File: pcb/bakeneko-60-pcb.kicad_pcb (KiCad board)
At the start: 2 copper layers, 284.8 x 106.7 mm, 150 parts, among them J1 JST SH 4-pin, J2 AVR-ISP-6, SW1 Reset, U1 SRV05-4, U2 ATmega32U4-AU, Y1 16MHz

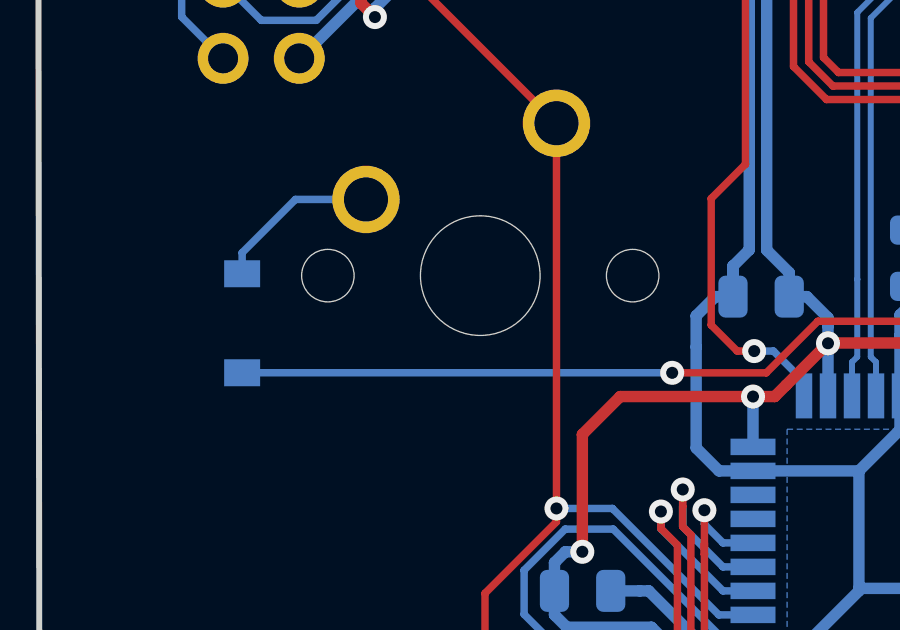
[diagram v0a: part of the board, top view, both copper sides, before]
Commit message: move diode and make room for jst replacement
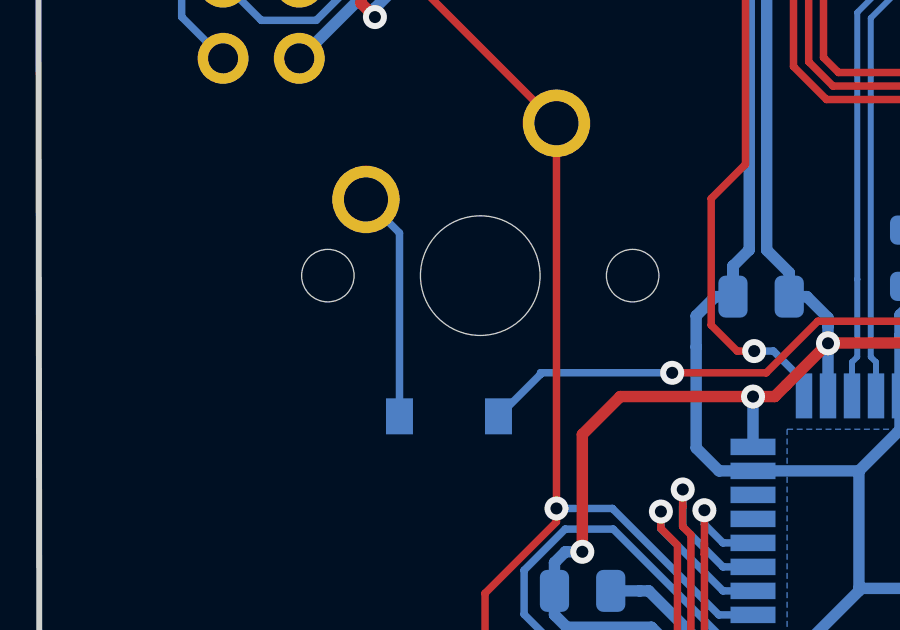
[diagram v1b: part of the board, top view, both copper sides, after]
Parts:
- moved D16 7.56 mm to (12.7, 32.7), turned to 180 degrees
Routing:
- net ROW1: track 261.0 -> 253.1 mm
- net Net-(D16-Pad2): track 5.56 -> 7.69 mm
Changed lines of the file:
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@@
   )
   (footprint "Diode_SMD:D_SOD-123" (layer "B.Cu")
-    (at 5.825 29.6375 90)
+    (at 12.72 32.74 180)
     (descr "SOD-123")
     (tags "SOD-123")
@@
     (property "Sheetname" "Switch Matrix")
     (attr smd)
-    (fp_text reference "D16" (at 0 -2 90) (layer "Dwgs.User")
+    (fp_text reference "D16" (at 0 -2) (layer "Dwgs.User")
       (effects (font (size 1 1) (thickness 0.15)) (justify mirror))
     )
-    (fp_text value "1N4148" (at 0 -2.1 90) (layer "B.Fab")
+    (fp_text value "1N4148" (at 0 -2.1) (layer "B.Fab")
       (effects (font (size 1 1) (thickness 0.15)) (justify mirror))
     )
-    (fp_text user "${REFERENCE}" (at 0 2 90) (layer "B.Fab")
+    (fp_text user "${REFERENCE}" (at 0 2) (layer "B.Fab")
       (effects (font (size 1 1) (thickness 0.15)) (justify mirror))
     )
@@
     (fp_line (start 1.4 0.9) (end 1.4 -0.9) (layer "B.Fab") (width 0.1))
     (fp_line (start -0.35 0) (end -0.35 -0.55) (layer "B.Fab") (width 0.1))
-    (pad "1" smd rect locked (at -1.65 0 90) (size 0.9 1.2) (layers "B.Cu" "B.Paste" "B.Mask")
+    (pad "1" smd rect locked (at -1.65 0 180) (size 0.9 1.2) (layers "B.Cu" "B.Paste" "B.Mask")
       (net 22 "ROW1") (pinfunction "K") (pintype "passive"))
-    (pad "2" smd rect locked (at 1.65 0 90) (size 0.9 1.2) (layers "B.Cu" "B.Paste" "B.Mask")
+    (pad "2" smd rect locked (at 1.65 0 180) (size 0.9 1.2) (layers "B.Cu" "B.Paste" "B.Mask")
       (net 20 "Net-(D16-Pad2)") (pinfunction "A") (pintype "passive"))
     (model "${KISYS3DMOD}/Diode_SMD.3dshapes/D_SOD-123.wrl"
@@
   (segment (start 258.55375 6.46) (end 256.49375 4.4) (width 0.25) (layer "B.Cu") (net 19))
   (segment (start 256.49375 4.4) (end 248.29375 4.4) (width 0.25) (layer "B.Cu") (net 19))
-  (segment (start 9.9525 25.51) (end 7.6025 25.51) (width 0.25) (layer "B.Cu") (net 20))
-  (segment (start 7.6025 25.51) (end 5.825 27.2875) (width 0.25) (layer "B.Cu") (net 20))
-  (segment (start 5.825 27.2875) (end 5.825 27.9875) (width 0.25) (layer "B.Cu") (net 20))
+  (segment (start 11.07 32.74) (end 11.07 26.6275) (width 0.25) (layer "B.Cu") (net 20))
+  (segment (start 11.07 26.6275) (end 9.9525 25.51) (width 0.25) (layer "B.Cu") (net 20))
   (segment (start 50.47375 25.51) (end 35.35599 25.51) (width 0.25) (layer "B.Cu") (net 21))
   (segment (start 53.50375 23.88) (end 52.10375 23.88) (width 0.25) (layer "B.Cu") (net 21))
@@
   (segment (start 37.435602 30.49375) (end 36.129352 31.8) (width 0.25) (layer "B.Cu") (net 22))
   (segment (start 34.25375 32.62875) (end 34.25375 33.75875) (width 0.25) (layer "B.Cu") (net 22))
+  (segment (start 15.7725 31.2875) (end 15.7725 31.3375) (width 0.25) (layer "B.Cu") (net 22))
   (segment (start 35.0825 31.8) (end 34.25375 32.62875) (width 0.25) (layer "B.Cu") (net 22))
   (segment (start 261.35 30.49375) (end 64.5625 30.49375) (width 0.25) (layer "B.Cu") (net 22))
   (segment (start 20.1575 31.2875) (end 20.16 31.29) (width 0.25) (layer "B.Cu") (net 22))
   (segment (start 261.39375 30.45) (end 261.35 30.49375) (width 0.25) (layer "B.Cu") (net 22))
-  (segment (start 5.825 31.2875) (end 20.1575 31.2875) (width 0.25) (layer "B.Cu") (net 22))
   (segment (start 35.0825 30.2925) (end 34.25 29.46) (width 0.25) (layer "B.Cu") (net 22))
+  (segment (start 15.7725 31.3375) (end 14.37 32.74) (width 0.25) (layer "B.Cu") (net 22))
   (segment (start 35.0825 31.8) (end 35.0825 30.2925) (width 0.25) (layer "B.Cu") (net 22))
   (segment (start 37.435602 30.49375) (end 64.5625 30.49375) (width 0.25) (layer "B.Cu") (net 22))
+  (segment (start 15.7725 31.2875) (end 20.1575 31.2875) (width 0.25) (layer "B.Cu") (net 22))
   (segment (start 36.129352 31.8) (end 35.0825 31.8) (width 0.25) (layer "B.Cu") (net 22))
   (segment (start 63.57875 25.51) (end 64.5625 26.49375) (width 0.25) (layer "B.Cu") (net 23))
@@
     )
   )
-  (group "" (id af2c1a3b-9986-4fa2-a3f2-ddb3c7ebb33d)
-    (members
-      e6c32500-66a0-4f4b-b0b9-a395d06f10b3
-    )
-  )

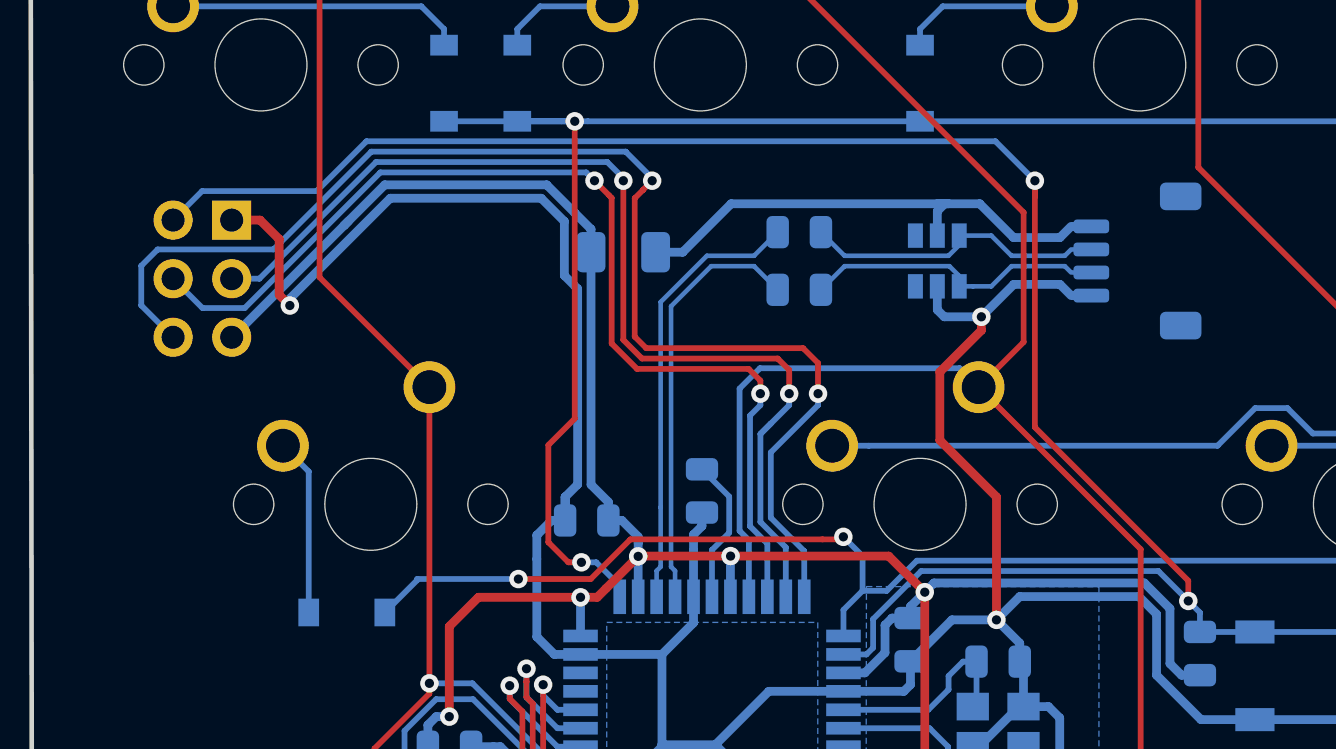
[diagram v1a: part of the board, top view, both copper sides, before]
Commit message: remove isp and connections
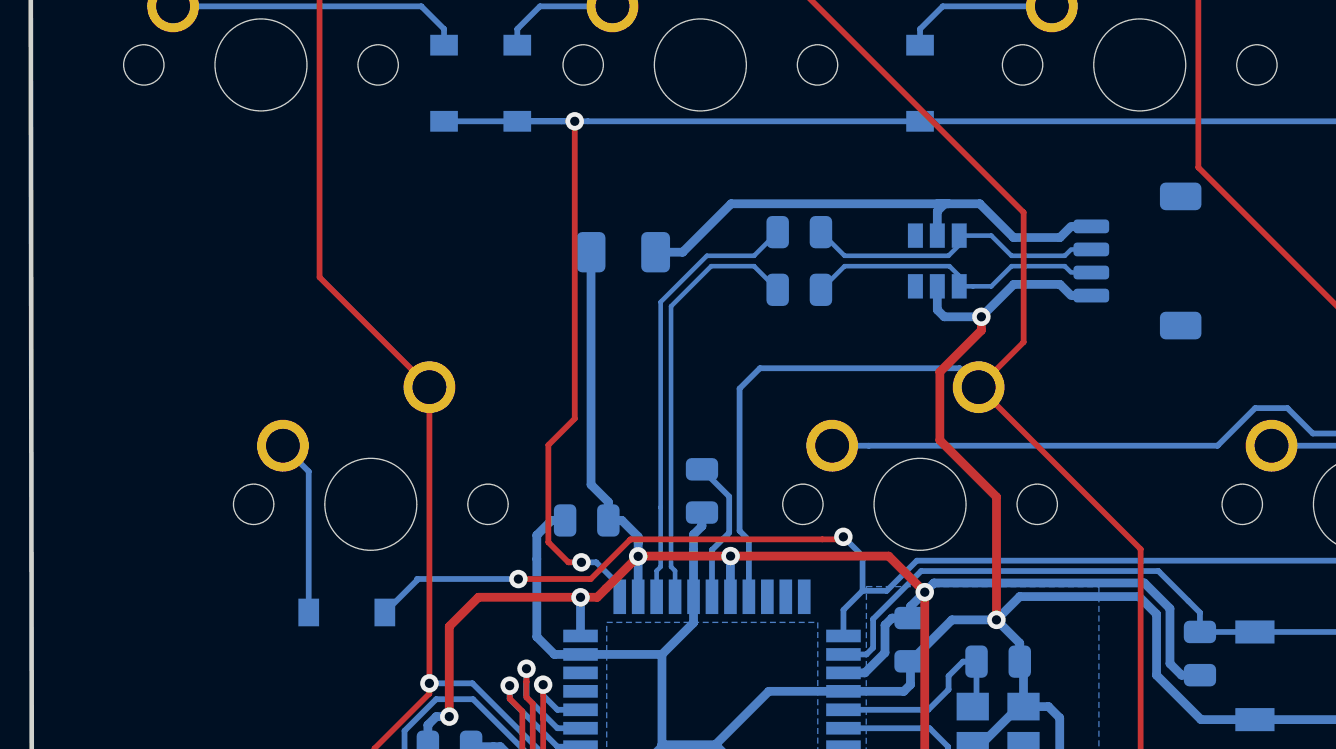
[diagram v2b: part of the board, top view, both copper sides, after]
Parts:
- removed J2: AVR-ISP-6, bakeneko:ISP
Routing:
- net RST: track 88.7 -> 28.0 mm, vias 2 -> 0
- net MISO: track 55.6 -> 0.00 mm, vias 2 -> 0
- net SCK: track 45.7 -> 0.00 mm, vias 2 -> 0
- net MOSI: track 45.6 -> 0.00 mm, vias 2 -> 0
- net GND: track 165.2 -> 130.9 mm, vias 5 -> 4
- net +5V: track 122.7 -> 102.3 mm

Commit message: move jst connector
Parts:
- moved J1 41.4 mm to (5.67, 20.3)
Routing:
- net GND: track 130.9 -> 191.3 mm
- net D+: track 13.2 -> 68.2 mm
- net D-: track 13.2 -> 58.2 mm
- net VBUS: track 22.6 -> 54.8 mm

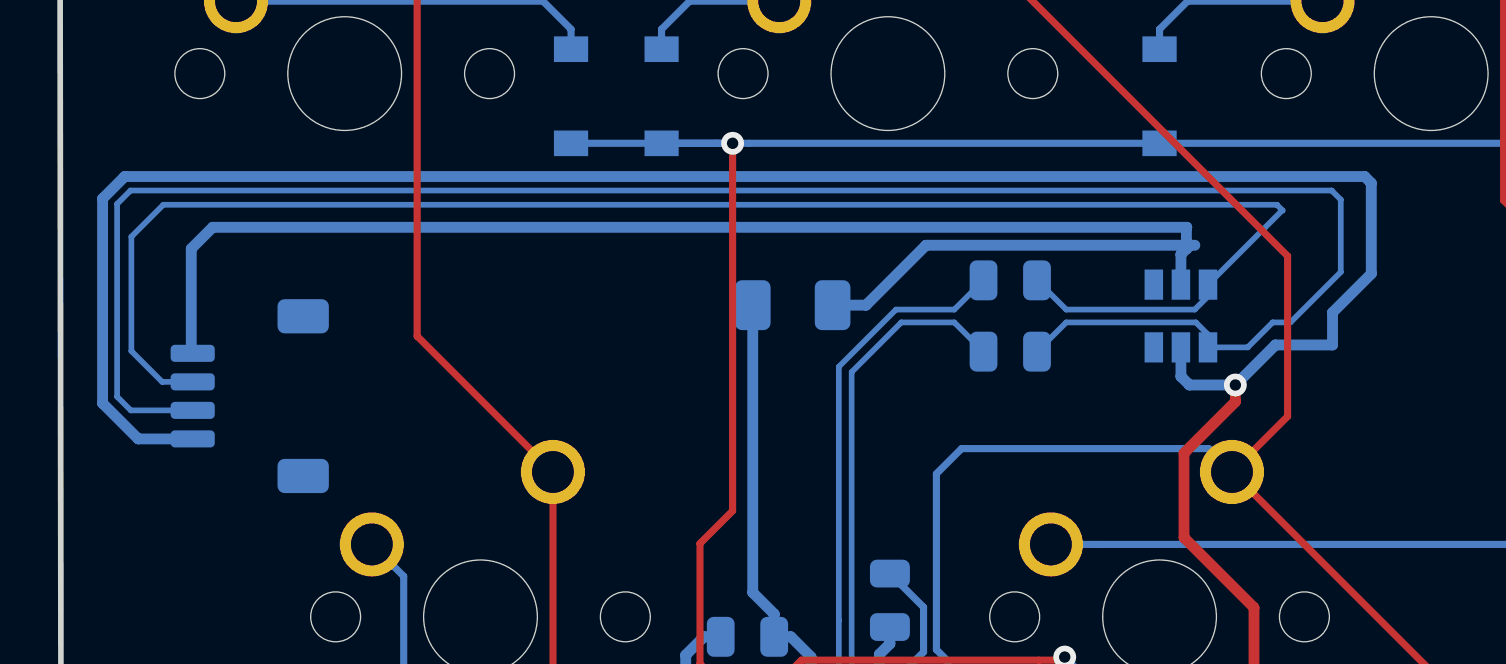
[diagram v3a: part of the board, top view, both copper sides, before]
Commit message: micro adjust placement of jst connector
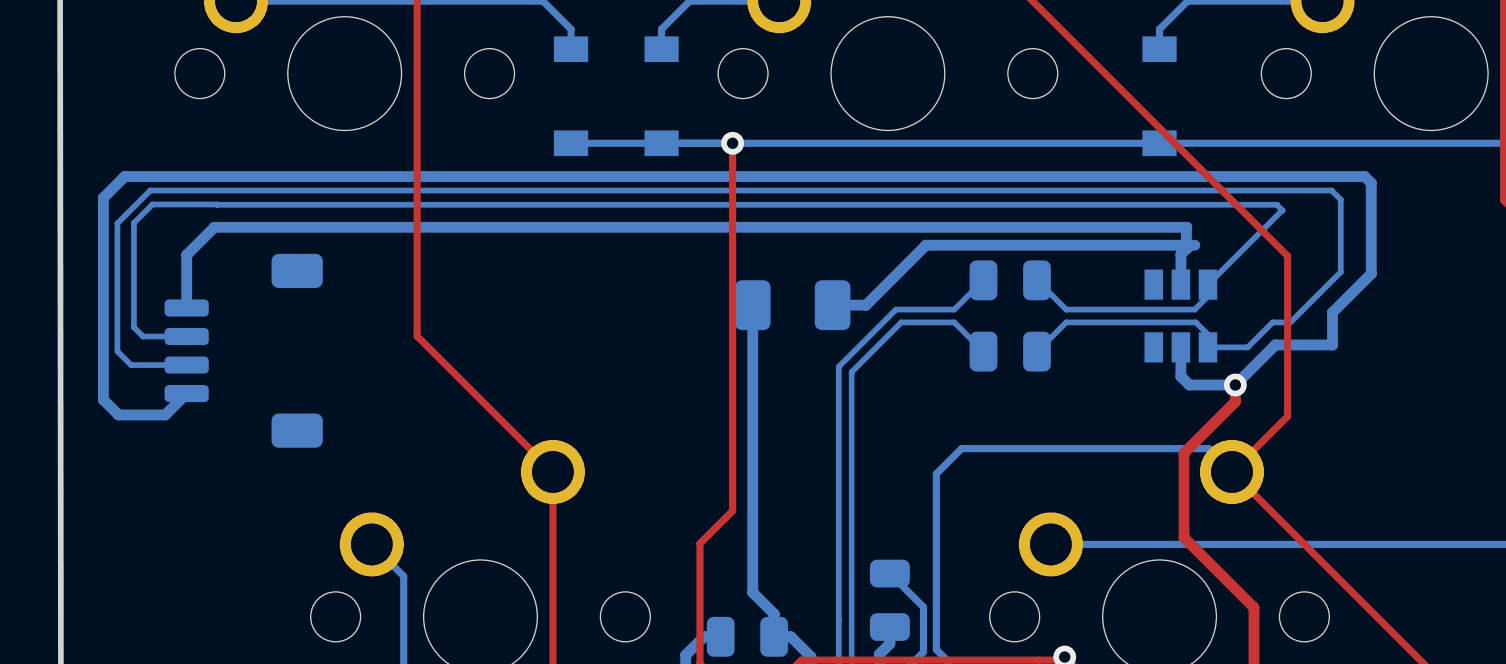
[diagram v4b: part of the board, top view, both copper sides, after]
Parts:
- moved J1 1.60 mm to (5.46, 18.7)
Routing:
- net D+: track 68.2 -> 66.0 mm
- net VBUS: track 54.8 -> 53.2 mm
- net D-: track 58.2 -> 57.0 mm

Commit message: cleanup tracks
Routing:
- net VBUS: track 53.2 -> 44.2 mm
- net D-: track 57.0 -> 52.0 mm
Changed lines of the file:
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@@
   (segment (start 262.34625 82.66) (end 261.3625 83.64375) (width 0.25) (layer "B.Cu") (net 71))
   (segment (start 267.1275 82.66) (end 262.34625 82.66) (width 0.25) (layer "B.Cu") (net 71))
-  (segment (start 38.32375 16.4) (end 38.32375 15.34) (width 0.381) (layer "B.Cu") (net 72))
-  (segment (start 38.516875 14.403125) (end 38.53 14.39) (width 0.381) (layer "B.Cu") (net 72))
-  (segment (start 38.53 14.39) (end 4.43 14.39) (width 0.381) (layer "B.Cu") (net 72))
+  (segment (start 26.11 17.12) (end 27.283694 17.12) (width 0.381) (layer "B.Cu") (net 72))
+  (segment (start 24.29 14.39) (end 4.43 14.39) (width 0.381) (layer "B.Cu") (net 72))
+  (segment (start 27.283694 17.12) (end 28.976847 15.426847) (width 0.381) (layer "B.Cu") (net 72))
+  (segment (start 38.32375 14.85375) (end 37.71 14.24) (width 0.381) (layer "B.Cu") (net 72))
+  (segment (start 28.976847 15.426847) (end 29.384311 15.019383) (width 0.381) (layer "B.Cu") (net 72))
+  (segment (start 30.163694 14.24) (end 28.976847 15.426847) (width 0.381) (layer "B.Cu") (net 72))
   (segment (start 4.43 14.39) (end 3.46 15.36) (width 0.381) (layer "B.Cu") (net 72))
-  (segment (start 38.814367 15.019383) (end 29.384311 15.019383) (width 0.381) (layer "B.Cu") (net 72))
-  (segment (start 38.516875 15.146875) (end 38.516875 14.403125) (width 0.381) (layer "B.Cu") (net 72))
-  (segment (start 27.283694 17.12) (end 26.11 17.12) (width 0.381) (layer "B.Cu") (net 72))
-  (segment (start 29.384311 15.019383) (end 27.283694 17.12) (width 0.381) (layer "B.Cu") (net 72))
+  (segment (start 37.71 14.24) (end 30.163694 14.24) (width 0.381) (layer "B.Cu") (net 72))
+  (segment (start 24.919383 15.019383) (end 24.29 14.39) (width 0.381) (layer "B.Cu") (net 72))
+  (segment (start 38.32375 16.4) (end 38.32375 14.85375) (width 0.381) (layer "B.Cu") (net 72))
+  (segment (start 29.384311 15.019383) (end 24.919383 15.019383) (width 0.381) (layer "B.Cu") (net 72))
   (segment (start 3.46 15.36) (end 3.46 17.22) (width 0.381) (layer "B.Cu") (net 72))
-  (segment (start 38.32375 15.34) (end 38.516875 15.146875) (width 0.381) (layer "B.Cu") (net 72))
-  (segment (start 38.516875 15.146875) (end 38.644367 15.019383) (width 0.381) (layer "B.Cu") (net 72))
   (segment (start 39.27375 18.15) (end 39.27375 18.6) (width 0.2) (layer "B.Cu") (net 73))
   (segment (start 39.27375 18.6) (end 40.665001 18.6) (width 0.2) (layer "B.Cu") (net 73))
@@
   (segment (start 41.540001 17.725) (end 42.165 17.725) (width 0.2) (layer "B.Cu") (net 73))
   (segment (start 1.03 18.74) (end 1.51 19.22) (width 0.2) (layer "B.Cu") (net 73))
-  (segment (start 1.93 18.22) (end 3.46 18.22) (width 0.2) (layer "B.Cu") (net 74))
-  (segment (start 41.89 13.8) (end 41.69 13.6) (width 0.2) (layer "B.Cu") (net 74))
-  (segment (start 1.61 14.24) (end 1.61 17.9) (width 0.2) (layer "B.Cu") (net 74))
-  (segment (start 4.526328 13.6) (end 4.516328 13.59) (width 0.2) (layer "B.Cu") (net 74))
-  (segment (start 41.69 13.6) (end 4.526328 13.6) (width 0.2) (layer "B.Cu") (net 74))
+  (segment (start 39.304867 13.514867) (end 4.545133 13.514867) (width 0.2) (layer "B.Cu") (net 74))
+  (segment (start 1.66 17.55) (end 2.33 18.22) (width 0.2) (layer "B.Cu") (net 74))
+  (segment (start 4.545133 13.514867) (end 1.66 16.4) (width 0.2) (layer "B.Cu") (net 74))
+  (segment (start 1.66 16.4) (end 1.66 17.55) (width 0.2) (layer "B.Cu") (net 74))
   (segment (start 34.3025 17.275) (end 38.80875 17.275) (width 0.2) (layer "B.Cu") (net 74))
-  (segment (start 39.27375 16.4) (end 41.87375 13.8) (width 0.2) (layer "B.Cu") (net 74))
-  (segment (start 2.26 13.59) (end 1.61 14.24) (width 0.2) (layer "B.Cu") (net 74))
+  (segment (start 39.304867 16.368883) (end 39.304867 13.514867) (width 0.2) (layer "B.Cu") (net 74))
   (segment (start 33.2775 16.25) (end 34.3025 17.275) (width 0.2) (layer "B.Cu") (net 74))
-  (segment (start 4.516328 13.59) (end 2.26 13.59) (width 0.2) (layer "B.Cu") (net 74))
   (segment (start 38.80875 17.275) (end 39.27375 16.81) (width 0.2) (layer "B.Cu") (net 74))
-  (segment (start 41.87375 13.8) (end 41.89 13.8) (width 0.2) (layer "B.Cu") (net 74))
-  (segment (start 1.61 17.9) (end 1.93 18.22) (width 0.2) (layer "B.Cu") (net 74))
+  (segment (start 39.27375 16.4) (end 39.304867 16.368883) (width 0.2) (layer "B.Cu") (net 74))
   (segment (start 39.27375 16.81) (end 39.27375 16.4) (width 0.2) (layer "B.Cu") (net 74))
+  (segment (start 2.33 18.22) (end 3.46 18.22) (width 0.2) (layer "B.Cu") (net 74))
   (segment (start 23.44625 61.07) (end 24.643741 59.872509) (width 0.25) (layer "F.Cu") (net 78))
   (segment (start 24.643741 59.872509) (end 24.643741 51.179221) (width 0.25) (layer "F.Cu") (net 78))
